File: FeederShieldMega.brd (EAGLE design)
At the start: 86.4 x 53.3 mm, 44 parts, among them J1 Digital_0_7, J10 Power, J2 Analog, J3 Digital_8_13, J4 Analog, J5 Digital_0_7, J6 Digital_22_36, J7 Digital_23_37, J8 Digital_38_52, J9 Digital_39_53, Q2 NTD5867NLT4G

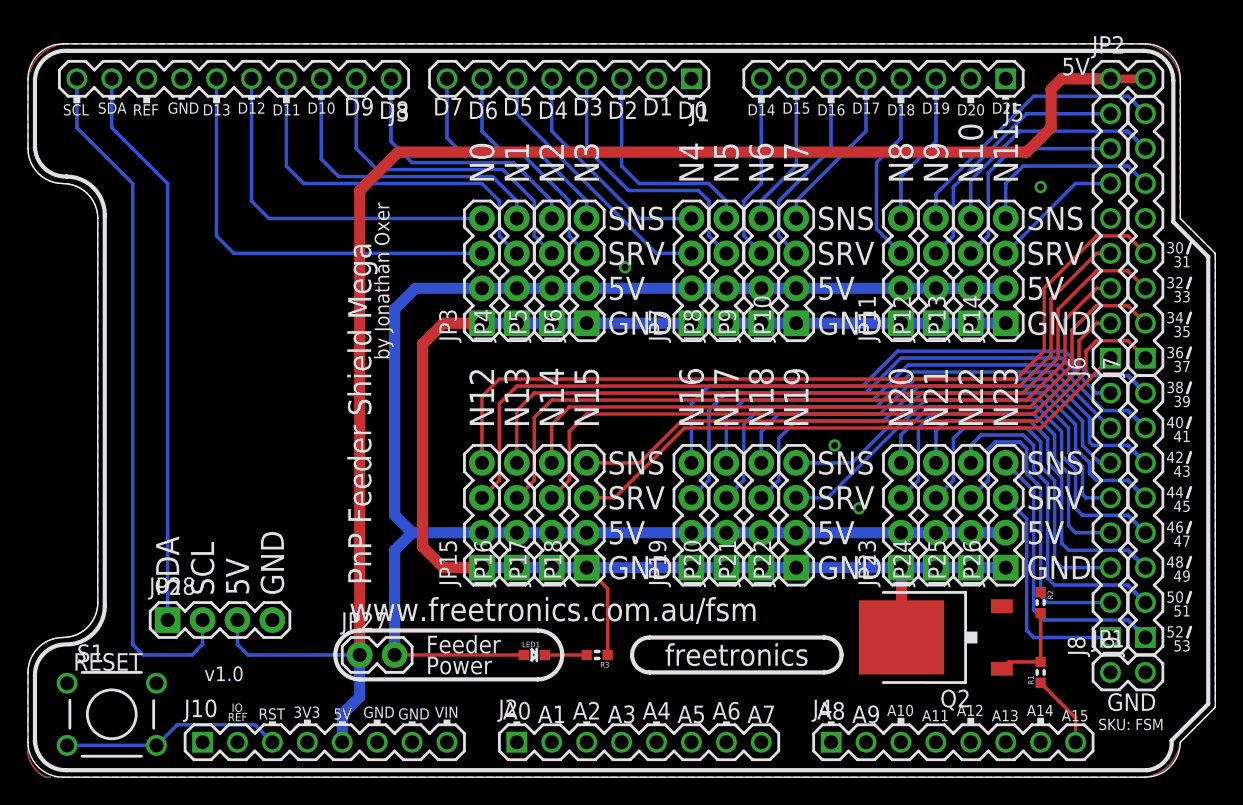
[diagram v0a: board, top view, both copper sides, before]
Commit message: Major rework to use 10-way IDC connections for v2.0 release
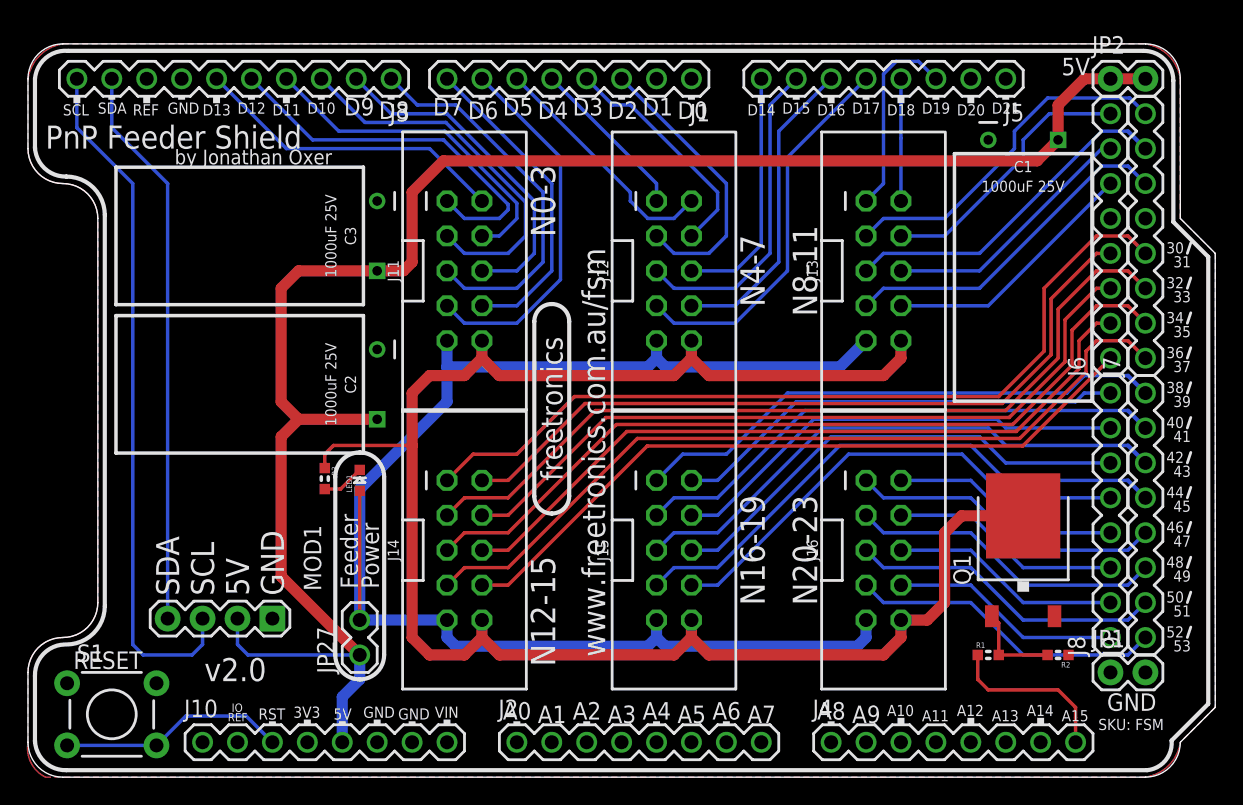
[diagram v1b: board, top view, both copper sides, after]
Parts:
- removed JP10: N7, freetronics-jon:1X04
- removed JP11: N8, freetronics-jon:1X04
- removed JP12: N9, freetronics-jon:1X04
- removed JP13: N10, freetronics-jon:1X04
- removed JP14: N11, freetronics-jon:1X04
- removed JP15: N12, freetronics-jon:1X04
- removed JP16: N13, freetronics-jon:1X04
- removed JP17: N14, freetronics-jon:1X04
- removed JP18: N15, freetronics-jon:1X04
- removed JP19: N16, freetronics-jon:1X04
- removed JP20: N17, freetronics-jon:1X04
- removed JP21: N18, freetronics-jon:1X04
- removed JP22: N19, freetronics-jon:1X04
- removed JP23, JP24, JP25, JP26: (no value), freetronics-jon:1X04
- removed JP28: OLED, freetronics-jon:1X04
- removed JP3: N0, freetronics-jon:1X04
- removed JP4: N1, freetronics-jon:1X04
- removed JP5: N2, freetronics-jon:1X04
- removed JP6: N3, freetronics-jon:1X04
- removed JP7: N4, freetronics-jon:1X04
- removed JP8: N5, freetronics-jon:1X04
- removed JP9: N6, freetronics-jon:1X04
- removed Q2: NTD5867NLT4G, freetronics-master-v1.1:DPACK
- added C1, C2, C3: 1000uF 25V, SuperHouse-DiscreteSemi:CPOL-RADIAL-5.08-10X18-FLAT
- added J11, J12, J13, J14, J15, J16: M02X5-SHROUDED, SuperHouse-Connectors:2X05-2.54-SHROUDED
- added MOD1: OLED-I2C128X32-0.91-HEADER, SuperHouse-Displays:OLED-128X32-0.91-HEADER
- added Q1: NTD5867NLT4G, SuperHouse-DiscreteSemi:DPACK
- J1, J5, J6, J7, J8, J9: device freetronics:1X08 -> SuperHouse-Connectors:1X08-P-BELOW
- J10, J2, J4: device freetronics-master-v1:1X08 -> SuperHouse-Connectors:1X08-P-BELOW
- J3: device freetronics-original:1X10 -> SuperHouse-Connectors:1X10-P-BELOW
- JP1, JP2: device freetronics-master-v1:1X02 -> SuperHouse-Connectors:1X02-P-BELOW
- JP27: device freetronics-jon:1X02 -> SuperHouse-Connectors:1X02-P
- LED1: device freetronics-jon:LED-0603 -> SuperHouse-LEDs:LED-0603
- R1, R2, R3: device freetronics-jon:0603 -> SuperHouse-DiscreteSemi:R0603
- S1: device freetronics-master-v1:TACTILE-PTH -> SuperHouse-Switches:TACTILE-PTH-6MM
- moved R3 23.6 mm to (21.6, 21.7), turned to 270 degrees
- moved LED1 18.0 mm to (24.1, 21.6), turned to 90 degrees
- moved R1 4.02 mm to (69.8, 8.89), turned to 0 degrees
- moved R2 4.02 mm to (74.9, 8.89), turned to 180 degrees
- turned JP27 to 90 degrees
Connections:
- removed net N$1: JP10.1, JP11.1, JP12.1, JP13.1, JP14.1, JP15.1, JP16.1, JP17.1, JP18.1, JP19.1, JP20.1, JP21.1, JP22.1, JP23.1, JP24.1, JP25.1, JP26.1, JP3.1, JP4.1, JP5.1, JP6.1, JP7.1, JP8.1, JP9.1, Q2.2, R3.1
- removed net N$2: JP10.2, JP11.2, JP12.2, JP13.2, JP14.2, JP15.2, JP16.2, JP17.2, JP18.2, JP19.2, JP20.2, JP21.2, JP22.2, JP23.2, JP24.2, JP25.2, JP26.2, JP27.2, JP3.2, JP4.2, JP5.2, JP6.2, JP7.2, JP8.2, JP9.2, LED1.A
- new net F_5V: J11.9, J12.9, J13.9, J14.9, J15.9, J16.9, JP27.2, LED1.A
- new net F_GND: J11.10, J12.10, J13.10, J14.10, J15.10, J16.10, Q1.2, R3.1
- net 5V: now also C1.1, C2.1, C3.1, MOD1.VCC; no longer JP28.3
- net D10: now also J11.3; no longer JP4.4
- net D11_MOSI: now also J11.4; no longer JP4.3
- net D12_MISO: now also J11.1; no longer JP3.4
- net D13_SCK: now also J11.2; no longer JP3.3
- net D14: now also J12.6; no longer JP9.3
- net D15: now also J12.5; no longer JP9.4
- net D16: now also J12.8; no longer JP10.3
- net D17: now also J12.7; no longer JP10.4
- net D18: now also J13.2; no longer JP11.3
- net D19: now also J13.1; no longer JP11.4
- net D2: now also J12.3; no longer JP8.4
- net D22: now also J13.4; no longer JP12.3
- net D23: now also J13.3; no longer JP12.4
- net D24: now also J13.6; no longer JP13.3
- net D25: now also J13.5; no longer JP13.4
- net D26: now also J13.8; no longer JP14.3
- net D27: now also J13.7; no longer JP14.4
- net D3: now also J12.4; no longer JP8.3
- net D30: now also J14.2; no longer JP15.3
- net D31: now also J14.1; no longer JP15.4
- net D32: now also J14.4; no longer JP16.3
- net D33: now also J14.3; no longer JP16.4
- net D34: now also J14.6; no longer JP17.3
- net D35: now also J14.5; no longer JP17.4
- net D36: now also J14.8; no longer JP18.3
- net D37: now also J14.7; no longer JP18.4
- net D38: now also J15.2; no longer JP19.3
- net D39: now also J15.1; no longer JP19.4
- net D4: now also J12.1; no longer JP7.4
- net D40: now also J15.4; no longer JP20.3
- net D41: now also J15.3; no longer JP20.4
- net D42: now also J15.6; no longer JP21.3
- net D43: now also J15.5; no longer JP21.4
- net D44: now also J15.8; no longer JP22.3
- net D45: now also J15.7; no longer JP22.4
- net D46: now also J16.2; no longer JP23.3
- net D47: now also J16.1; no longer JP23.4
- net D48: now also J16.4; no longer JP24.3
- net D49: now also J16.3; no longer JP24.4
- net D5: now also J12.2; no longer JP7.3
- net D50_MISO: now also J16.6; no longer JP25.3
- net D51_MOSI: now also J16.5; no longer JP25.4
- net D52_SCK: now also J16.8; no longer JP26.3
- net D53: now also J16.7; no longer JP26.4
- net D6: now also J11.7; no longer JP6.4
- net D7: now also J11.8; no longer JP6.3
- net D8: now also J11.5; no longer JP5.4
- net D9: now also J11.6; no longer JP5.3
- net GND: now also C1.2, C2.2, C3.2, MOD1.GND, Q1.3; no longer JP28.4, Q2.3
- net N$3: now also Q1.1; no longer Q2.1
- net SCL: now also MOD1.SCL; no longer JP28.2
- net SDA: now also MOD1.SDA; no longer JP28.1
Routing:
- net F_GND: track 0.00 -> 125.8 mm
- net N$2: track 123.9 -> 0.00 mm
- net N$1: track 112.9 -> 0.00 mm
- net F_5V: track 0.00 -> 107.1 mm
- net D17: track 12.3 -> 28.0 mm
- net D37: track 45.8 -> 59.6 mm
- net 5V: track 113.8 -> 127.4 mm
- net D6: track 14.8 -> 27.1 mm
- net D15: track 11.2 -> 23.3 mm
- net D27: track 13.8 -> 25.1 mm
- net D36: track 42.3 -> 52.6 mm
- net D46: track 26.8 -> 16.8 mm
- net D26: track 9.72 -> 18.9 mm
- net D45: track 32.1 -> 41.3 mm
- net D35: track 51.6 -> 60.2 mm
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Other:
- board text added: "Copyright 2018-2020 Freetronics Pty Ltd Released under the TAPR Open Hardware License: www.tapr.org/OHL"
- board text added: "N0-3"
- board text added: "N12-15"
- board text added: "N16-19"
- board text added: "N20-23"
- board text added: "N4-7"
- board text added: "N8-11"
- board text added: "PnP Feeder Shield"
- board text added: "v2.0"
- board text removed: "(C) 2018"
- board text removed: "Copyright 2018 Freetronics Pty Ltd Released under the TAPR Open Hardware License: www.tapr.org/OHL"
- board text removed: "Freetronics"
- board text removed: "N0"
- board text removed: "N1"
- board text removed: "N10"
- board text removed: "N11"
- board text removed: "N12"
- board text removed: "N13"
- board text removed: "N14"
- board text removed: "N15"
- board text removed: "N16"
- board text removed: "N17"
- board text removed: "N18"
- board text removed: "N19"
- board text removed: "N2"
- board text removed: "N20"
- board text removed: "N21"
- board text removed: "N22"
- board text removed: "N23"
- board text removed: "N3"
- board text removed: "N4"
- board text removed: "N5"
- board text removed: "N6"
- board text removed: "N7"
- board text removed: "N8"
- board text removed: "N9"
- board text removed: "PnP Feeder Shield Mega"
- board text removed: "SNS"
- board text removed: "SRV"
- board text removed: "v1.0"
